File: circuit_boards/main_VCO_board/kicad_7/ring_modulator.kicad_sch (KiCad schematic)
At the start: 20 parts, among them U13 NE5532, U14 TL072

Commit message: Progress on circuit boards
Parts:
- C803: value 100p -> 10p
- R803, R804: value 100k -> 33k
- R808: value 100k -> 560k
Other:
- note removed: "TODO attenuate at the input some"
- moved on the sheet: TR802

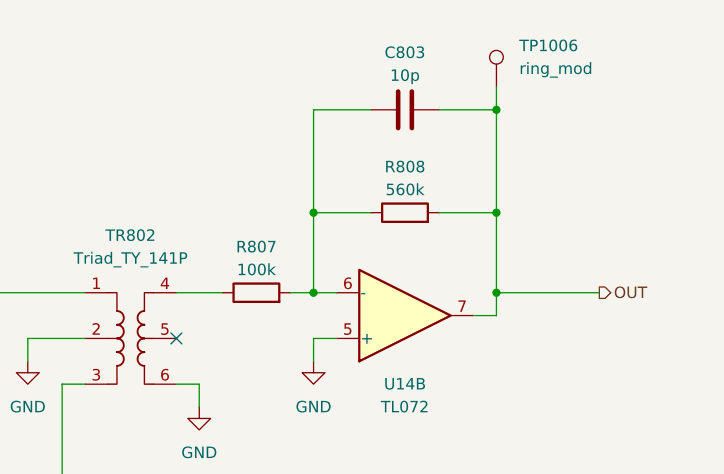
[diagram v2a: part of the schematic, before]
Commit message: Resistor tweaks while evaluating 1st build
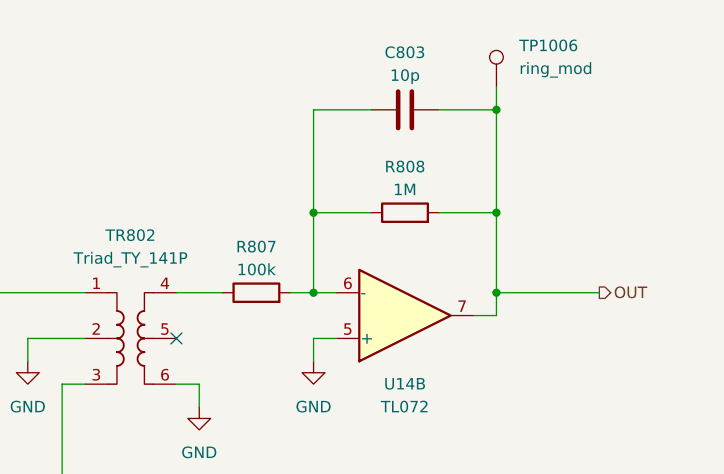
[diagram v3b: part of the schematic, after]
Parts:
- R808: value 560k -> 1M
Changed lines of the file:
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@@
       (effects (font (size 1.27 1.27)))
     )
-    (property "Value" "560k" (at 215.9 72.39 90)
+    (property "Value" "1M" (at 215.9 72.39 90)
       (effects (font (size 1.27 1.27)))
     )
